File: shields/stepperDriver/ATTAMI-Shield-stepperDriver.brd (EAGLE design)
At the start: 22.8 x 33 mm, 12 parts

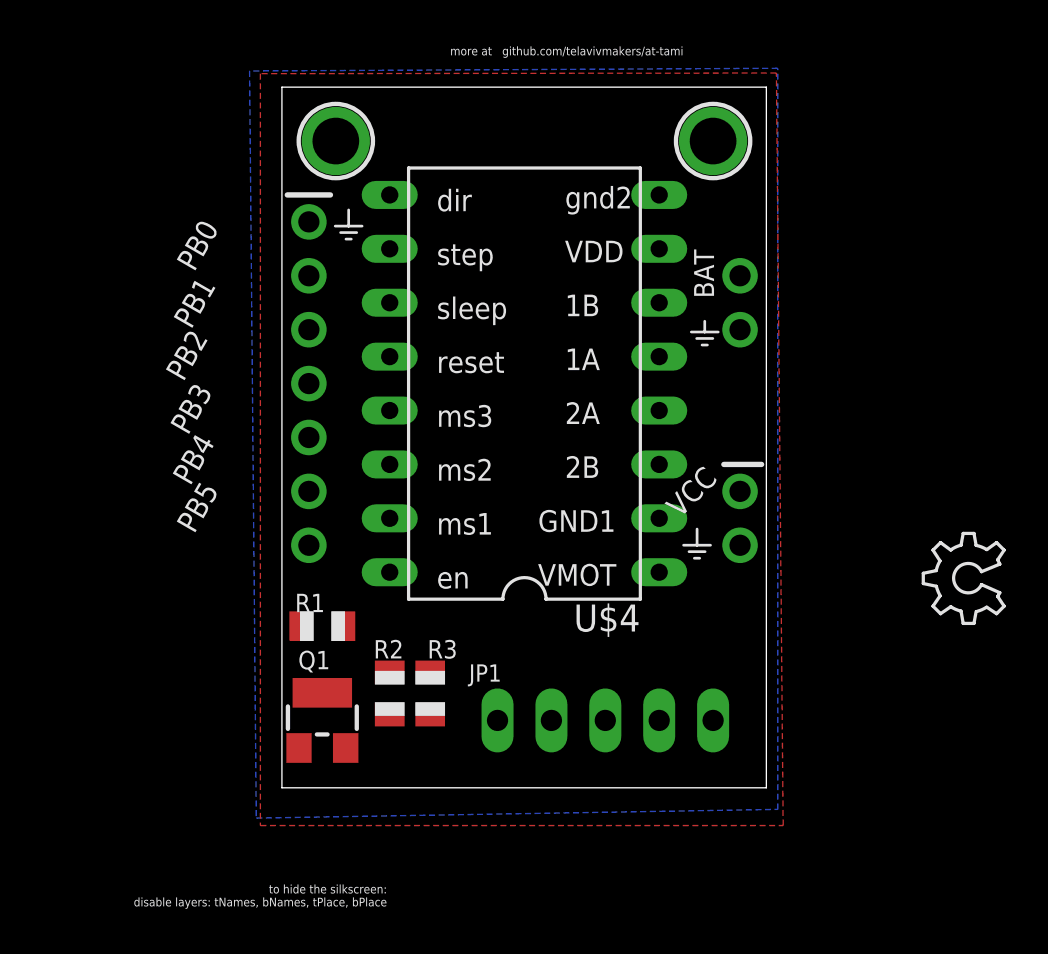
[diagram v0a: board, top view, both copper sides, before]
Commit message: cont work on stepper shield
mostly done, could work if we agree on V_BAT to 12V
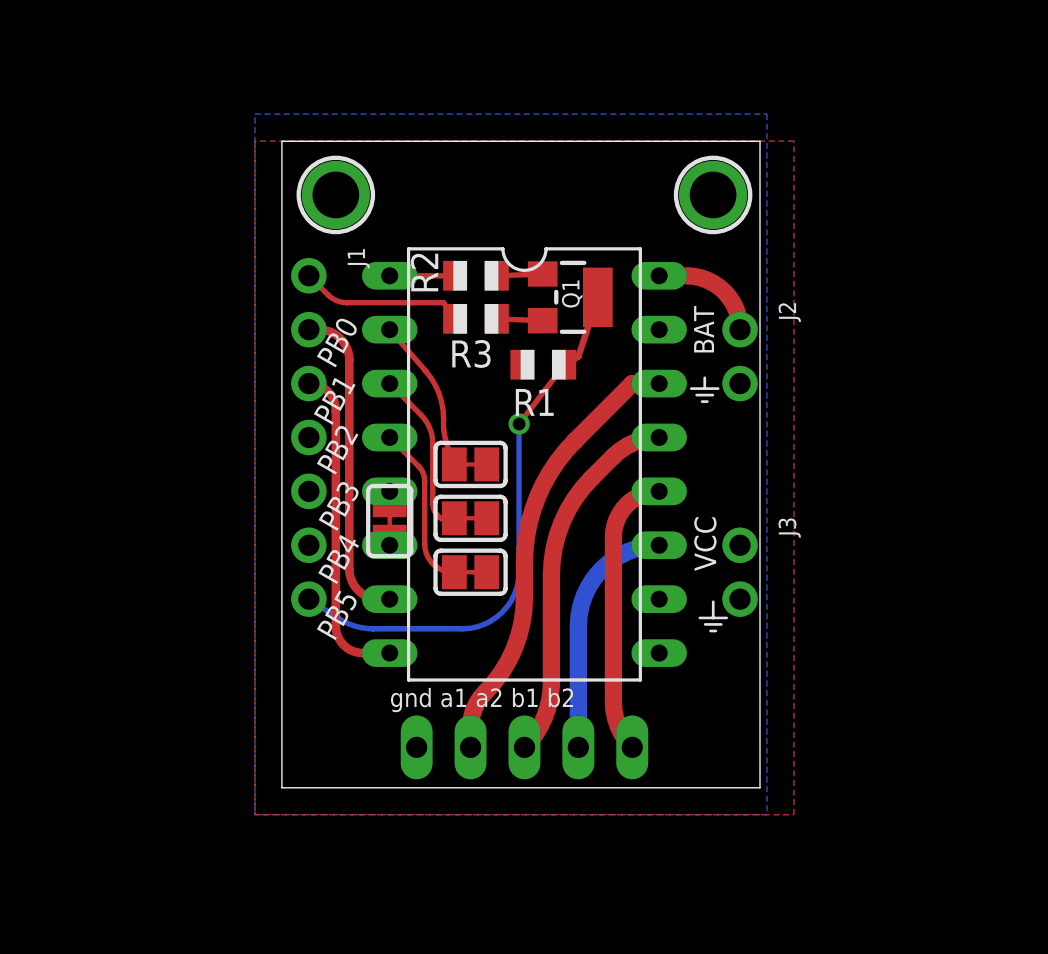
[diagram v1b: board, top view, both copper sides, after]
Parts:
- removed U$4: POLOLUESTEPPERDRIVER, reprap:DIL16
- added SJ1, SJ2, SJ3, SJ4: (no value), microbuilder:SOLDERJUMPER_CLOSEDWIRE
- U$3: value (none) -> STEPPER_driver; device ohw-logo:OSHW_6X150_NOTEXT -> ATtami:DIL16
- moved U$3 23.8 mm to (11.4, 15.2), turned to 0 degrees
- moved Q1 23.1 mm to (13.6, 23.1), turned to 270 degrees
- moved R2 20.1 mm to (9.14, 24.1), turned to 0 degrees
- moved U$1 18.0 mm to (20.3, 27.9), turned to 0 degrees
- moved U$2 18.0 mm to (2.54, 27.9)
- moved R3 17.8 mm to (9.14, 22.1), turned to 0 degrees
- moved R1 16.1 mm to (12.3, 19.9), turned to 0 degrees
- moved JP1 4.02 mm to (11.4, 1.91)
- moved J1 2.54 mm to (1.27, 16.5)
- moved J2 2.54 mm to (21.6, 20.3)
- moved J3 2.54 mm to (21.6, 10.2)
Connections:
- removed net EN: R2.1, U$4.16
- removed net N$11: JP1.2, U$4.5
- new net ENABLE: R2.1, U$3.1
- new net N$14: SJ1.2, U$3.4
- new net N$2: SJ4.2, U$3.5
- new net N$3: JP1.2, U$3.11
- new net N$6: JP1.3, U$3.12
- new net N$7: JP1.4, U$3.14
- new net N$9: SJ4.1, U$3.6
- net GND: now also JP1.1, U$3.10, U$3.16; no longer U$4.2, U$4.8
- net N$10: now also SJ3.2, U$3.2; no longer JP1.3, U$4.4
- net N$13: now also SJ2.2, U$3.3; no longer JP1.1, U$4.6
- net N$8: now also JP1.5, U$3.13; no longer JP1.4, U$4.3
- net PB0: now also U$3.7; no longer U$4.9
- net PB1: now also U$3.8; no longer U$4.10
- net VCC: now also SJ1.1, SJ2.1, SJ3.1, U$3.15; no longer U$4.7
- net V_BAT: now also U$3.9; no longer JP1.5, U$4.1
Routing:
- net PB5: track 0.00 -> 25.5 mm, vias 0 -> 1
- net N$3: track 0.00 -> 21.1 mm
- net N$6: track 0.00 -> 17.1 mm
- net PB1: track 0.00 -> 15.0 mm
- net PB0: track 0.00 -> 14.8 mm
- net N$8: track 0.00 -> 13.1 mm
- net N$7: track 0.00 -> 11.1 mm
- net N$13: track 0.00 -> 7.77 mm
- net GND: track 0.00 -> 7.72 mm
- net N$14: track 0.00 -> 7.59 mm
- net N$10: track 0.00 -> 7.21 mm
- net V_BAT: track 0.00 -> 3.59 mm
- net ENABLE: track 0.00 -> 3.06 mm
- net N$5: track 0.00 -> 2.15 mm
- net N$4: track 0.00 -> 2.15 mm
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- added copper zone on layer 1, net VCC
- removed copper zone on layer 1, net GND
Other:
- board size 22.8 x 33 mm -> 22.5 x 30.5 mm
- board text added: "gnd a1 a2 b1 b2"
- board text removed: "+"
- board text removed: "1A"
- board text removed: "1B"
- board text removed: "2A"
- board text removed: "2B"
- board text removed: "GND1"
- board text removed: "J2"
- board text removed: "VDD"
- board text removed: "VMOT"
- board text removed: "dir"
- board text removed: "en"
- board text removed: "gnd2"
- board text removed: "more at github.com/telavivmakers/at-tami"
- board text removed: "ms1"
- board text removed: "ms2"
- board text removed: "ms3"
- board text removed: "reset"
- board text removed: "sleep"
- board text removed: "step"
- board text removed: "to hide the silkscreen: disable layers: tNames, bNames, tPlace, bPlace"

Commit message: updtae A4988 lib part
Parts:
- BRK1: value STEPPER_driver -> A4988_driver
- moved R1 2.68 mm to (9.65, 19.7)
- moved R3 0.52 mm to (9.65, 22.0)
- moved R2 0.40 mm to (9.53, 24.3)
- renumbered U$3 to BRK1
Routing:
- net PB5: track 25.5 -> 27.0 mm
- net N$4: track 2.15 -> 1.64 mm
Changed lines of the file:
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@@
 <attribute name="VALUE" x="12.954" y="21.082" size="0.4064" layer="27" ratio="10" rot="R270"/>
 </element>
-<element name="R1" library="adafruit" package="R0805" value="" x="12.319" y="19.939" smashed="yes">
-<attribute name="NAME" x="12.954" y="18.796" size="1.27" layer="25" rot="R180"/>
-<attribute name="VALUE" x="11.557" y="17.653" size="1.27" layer="27"/>
-</element>
-<element name="R2" library="adafruit" package="R0805" value="" x="9.144" y="24.13" smashed="yes">
-<attribute name="NAME" x="7.366" y="23.241" size="1.27" layer="25" rot="R90"/>
-<attribute name="VALUE" x="8.382" y="21.844" size="1.27" layer="27"/>
-</element>
-<element name="R3" library="adafruit" package="R0805" value="" x="9.144" y="22.098" smashed="yes">
-<attribute name="NAME" x="7.874" y="19.812" size="1.27" layer="25"/>
-<attribute name="VALUE" x="8.382" y="19.812" size="1.27" layer="27"/>
+<element name="R1" library="adafruit" package="R0805" value="" x="9.652" y="19.685" smashed="yes">
+<attribute name="NAME" x="11.811" y="20.701" size="1.016" layer="25" rot="R270"/>
+<attribute name="VALUE" x="8.89" y="17.399" size="1.27" layer="27"/>
+</element>
+<element name="R2" library="adafruit" package="R0805" value="" x="9.525" y="24.257" smashed="yes">
+<attribute name="NAME" x="7.874" y="23.495" size="1.016" layer="25" rot="R90"/>
+<attribute name="VALUE" x="8.763" y="21.971" size="1.27" layer="27"/>
+</element>
+<element name="R3" library="adafruit" package="R0805" value="" x="9.652" y="21.971" smashed="yes">
+<attribute name="NAME" x="7.874" y="21.336" size="1.016" layer="25" rot="R90"/>
+<attribute name="VALUE" x="8.89" y="19.685" size="1.27" layer="27"/>
 </element>
 <element name="SJ1" library="microbuilder" package="SOLDERJUMPER_CLOSEDWIRE" value="" x="8.89" y="10.16" smashed="yes" rot="R180">
@@
 <element name="U$1" library="microbuilder" package="MOUNTINGHOLE_2.0_PLATED" value="MOUNTINGHOLE2.0" x="20.32" y="27.94"/>
 <element name="U$2" library="microbuilder" package="MOUNTINGHOLE_2.0_PLATED" value="MOUNTINGHOLE2.0" x="2.54" y="27.94"/>
-<element name="U$3" library="ATtami" package="DIL16" value="STEPPER_driver" x="11.43" y="15.24" smashed="yes">
+<element name="BRK1" library="ATtami" package="DIL16" value="A4988_driver" x="11.43" y="15.24" smashed="yes">
 <attribute name="VALUE" x="15.875" y="5.334" size="1.27" layer="27" ratio="10" rot="R90"/>
 </element>
@@
 <contactref element="J1" pad="1"/>
 <contactref element="R3" pad="1"/>
-<contactref element="U$3" pad="16"/>
+<contactref element="BRK1" pad="16"/>
 <polygon width="0.4064" layer="16">
 <vertex x="-1.27" y="31.75"/>
@@
 <vertex x="-1.27" y="-1.27"/>
 </polygon>
-<wire x1="7.62" y1="22.86" x2="3.06605" y2="22.86" width="0.254" layer="1"/>
+<wire x1="3.06605" y1="22.86" x2="6.975896875" y2="22.86" width="0.254" layer="1"/>
+<wire x1="6.975896875" y1="22.86" x2="8.00054375" y2="22.34033125" width="0.254" layer="1" curve="-53.785325"/>
+<wire x1="8.00054375" y1="22.34033125" x2="8.652" y2="21.971" width="0.254" layer="1"/>
 <wire x1="3.06605" y1="22.86" x2="2.168025" y2="23.231975" width="0.254" layer="1" curve="-45"/>
 <wire x1="2.168025" y1="23.231975" x2="1.27" y2="24.13" width="0.254" layer="1"/>
-<contactref element="U$3" pad="10"/>
+<contactref element="BRK1" pad="10"/>
 <contactref element="JP1" pad="1"/>
-<wire x1="7.62" y1="22.86" x2="8.144" y2="22.098" width="0.254" layer="1"/>
 </signal>
 <signal name="VCC">
 <contactref element="J3" pad="1"/>
 <contactref element="R1" pad="1"/>
-<contactref element="U$3" pad="15"/>
+<contactref element="BRK1" pad="15"/>
 <contactref element="SJ1" pad="1"/>
 <contactref element="SJ2" pad="1"/>
@@
 <contactref element="J2" pad="1"/>
 <wire x1="19.05" y1="24.13" x2="21.59" y2="21.59" width="0.8128" layer="1" curve="-90"/>
-<contactref element="U$3" pad="9"/>
+<contactref element="BRK1" pad="9"/>
 <wire x1="17.78" y1="24.13" x2="19.05" y2="24.13" width="0" layer="19" extent="1-1"/>
 </signal>
 <signal name="PB0">
 <contactref element="J1" pad="2"/>
-<contactref element="U$3" pad="7"/>
+<contactref element="BRK1" pad="7"/>
 <wire x1="1.27" y1="21.59" x2="1.755096875" y2="21.59" width="0.4064" layer="1"/>
 <wire x1="1.755096875" y1="21.59" x2="3.175" y2="20.170096875" width="0.4064" layer="1" curve="-90"/>
@@
 <signal name="PB1">
 <contactref element="J1" pad="3"/>
-<contactref element="U$3" pad="8"/>
+<contactref element="BRK1" pad="8"/>
 <wire x1="1.27" y1="19.05" x2="2.54" y2="17.78" width="0.4064" layer="1" curve="-90"/>
 <wire x1="2.54" y1="17.78" x2="2.54" y2="7.62" width="0.4064" layer="1"/>
@@
 <contactref element="Q1" pad="3"/>
 <contactref element="J1" pad="7"/>
-<wire x1="13.319" y1="19.939" x2="11.176" y2="17.145" width="0.254" layer="1"/>
+<wire x1="10.652" y1="19.685" x2="11.176" y2="17.145" width="0.254" layer="1"/>
 <via x="11.176" y="17.145" extent="1-16" drill="0.6" shape="square"/>
 <wire x1="11.176" y1="17.145" x2="11.176" y2="10.172065625" width="0.254" layer="16"/>
@@
 <wire x1="4.292428125" y1="7.493" x2="2.704090625" y2="7.962059375" width="0.254" layer="16" curve="-32.905279"/>
 <wire x1="2.704090625" y1="7.962059375" x2="1.27" y2="8.89" width="0.254" layer="16"/>
-<wire x1="14.889" y1="23.114" x2="13.97" y2="20.32" width="0.3048" layer="1"/>
-<wire x1="13.97" y1="20.32" x2="13.319" y2="19.939" width="0.3048" layer="1"/>
+<wire x1="14.889" y1="23.114" x2="14.3002875" y2="21.324159375" width="0.3048" layer="1"/>
+<wire x1="14.3002875" y1="21.324159375" x2="12.931759375" y2="20.1213" width="0.3048" layer="1" curve="-60.958763"/>
+<wire x1="12.931759375" y1="20.1213" x2="10.652" y2="19.685" width="0.3048" layer="1"/>
 </signal>
 <signal name="N$4">
 <contactref element="R3" pad="2"/>
 <contactref element="Q1" pad="2"/>
-<wire x1="12.289" y1="22.014" x2="10.144" y2="22.098" width="0.254" layer="1"/>
+<wire x1="12.289" y1="22.014" x2="10.652" y2="21.971" width="0.254" layer="1"/>
 </signal>
 <signal name="N$5">
 <contactref element="Q1" pad="1"/>
 <contactref element="R2" pad="2"/>
-<wire x1="10.144" y1="24.13" x2="12.289" y2="24.214" width="0.254" layer="1"/>
+<wire x1="10.525" y1="24.257" x2="12.289" y2="24.214" width="0.254" layer="1"/>
 </signal>
 <signal name="ENABLE">
 <contactref element="R2" pad="1"/>
-<contactref element="U$3" pad="1"/>
-<wire x1="5.08" y1="24.13" x2="8.144" y2="24.13" width="0.254" layer="1"/>
+<contactref element="BRK1" pad="1"/>
+<wire x1="5.08" y1="24.13" x2="8.525" y2="24.257" width="0.254" layer="1"/>
 </signal>
 <signal name="N$10">
 <contactref element="SJ3" pad="2"/>
-<contactref element="U$3" pad="2"/>
+<contactref element="BRK1" pad="2"/>
 <wire x1="8.128" y1="15.24" x2="8.063171875" y2="15.434484375" width="0.254" layer="1"/>
 <wire x1="8.063171875" y1="15.434484375" x2="7.62" y2="16.89543125" width="0.254" layer="1" curve="-18.434976"/>
@@
 <signal name="N$13">
 <contactref element="SJ2" pad="2"/>
-<contactref element="U$3" pad="3"/>
+<contactref element="BRK1" pad="3"/>
 <wire x1="8.128" y1="12.7" x2="7.92519375" y2="12.573" width="0.254" layer="1"/>
 <wire x1="7.92519375" y1="12.573" x2="7.112" y2="13.38619375" width="0.254" layer="1" curve="-90"/>
@@
 <signal name="N$14">
 <contactref element="SJ1" pad="2"/>
-<contactref element="U$3" pad="4"/>
+<contactref element="BRK1" pad="4"/>
 <wire x1="5.08" y1="16.51" x2="6.4477125" y2="15.1422875" width="0.254" layer="1"/>
 <wire x1="6.4477125" y1="15.1422875" x2="6.731" y2="14.458371875" width="0.254" layer="1" curve="-45"/>
@@
 <signal name="N$3">
 <contactref element="JP1" pad="2"/>
-<contactref element="U$3" pad="11"/>
+<contactref element="BRK1" pad="11"/>
 <wire x1="17.78" y1="19.05" x2="16.51" y2="19.05" width="0.8128" layer="1"/>
 <wire x1="16.51" y1="19.05" x2="13.811796875" y2="16.351796875" width="0.8128" layer="1"/>
@@
 <signal name="N$6">
 <contactref element="JP1" pad="3"/>
-<contactref element="U$3" pad="12"/>
+<contactref element="BRK1" pad="12"/>
 <wire x1="17.78" y1="16.51" x2="15.611975" y2="15.611975" width="0.8128" layer="1" curve="45"/>
 <wire x1="15.611975" y1="15.611975" x2="14.596703125" y2="14.596703125" width="0.8128" layer="1"/>
@@
 <signal name="N$7">
 <contactref element="JP1" pad="4"/>
-<contactref element="U$3" pad="14"/>
+<contactref element="BRK1" pad="14"/>
 <wire x1="17.78" y1="11.43" x2="13.97" y2="7.62" width="0.8128" layer="16" curve="90"/>
 <wire x1="13.97" y1="7.62" x2="13.97" y2="1.905" width="0.8128" layer="16"/>
@@
 <signal name="N$8">
 <contactref element="JP1" pad="5"/>
-<contactref element="U$3" pad="13"/>
+<contactref element="BRK1" pad="13"/>
 <wire x1="17.78" y1="13.97" x2="15.621" y2="11.811" width="0.8128" layer="1" curve="90"/>
 <wire x1="15.621" y1="11.811" x2="15.621" y2="4.051234375" width="0.8128" layer="1"/>
@@
 </signal>
 <signal name="N$2">
-<contactref element="U$3" pad="5"/>
+<contactref element="BRK1" pad="5"/>
 <contactref element="SJ4" pad="2"/>
 <wire x1="5.08" y1="13.335" x2="5.08" y2="13.97" width="0.4064" layer="1"/>
@@
 <signal name="N$9">
 <contactref element="SJ4" pad="1"/>
-<contactref element="U$3" pad="6"/>
+<contactref element="BRK1" pad="6"/>
 <wire x1="5.08" y1="11.43" x2="5.08" y2="11.811" width="0.4064" layer="1"/>
 </signal>

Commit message: addded 4pin header for 12+ and I2C, not routed
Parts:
- added CN1: 1X4-BIG, adafruit:1X04-BIG
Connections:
- net GND: now also CN1.2
- net PB3: now also CN1.4
- net PB4: now also CN1.3
- net V_BAT: now also CN1.1
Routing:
- net V_BAT: track 3.59 -> 8.17 mm
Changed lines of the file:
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@@
 <attribute name="VALUE" x="6.731" y="11.049" size="0.4064" layer="27" ratio="10" rot="R90"/>
 </element>
+<element name="CN1" library="adafruit" package="1X04-BIG" value="1X4-BIG" x="15.24" y="27.94" smashed="yes" rot="R180"/>
 </elements>
 <signals>
@@
 <contactref element="BRK1" pad="10"/>
 <contactref element="JP1" pad="1"/>
+<contactref element="CN1" pad="2"/>
 </signal>
 <signal name="VCC">
@@
 <wire x1="19.05" y1="24.13" x2="21.59" y2="21.59" width="0.8128" layer="1" curve="-90"/>
 <contactref element="BRK1" pad="9"/>
+<contactref element="CN1" pad="1"/>
+<wire x1="15.24" y1="27.94" x2="17.78" y2="24.13" width="0.8128" layer="1"/>
 <wire x1="17.78" y1="24.13" x2="19.05" y2="24.13" width="0" layer="19" extent="1-1"/>
 </signal>
@@
 <signal name="PB3">
 <contactref element="J1" pad="5"/>
+<contactref element="CN1" pad="4"/>
+<wire x1="1.27" y1="13.97" x2="7.62" y2="27.94" width="0" layer="19" extent="1-1"/>
 </signal>
 <signal name="PB4">
 <contactref element="J1" pad="6"/>
+<contactref element="CN1" pad="3"/>
+<wire x1="1.27" y1="11.43" x2="10.16" y2="27.94" width="0" layer="19" extent="1-1"/>
 </signal>
 <signal name="PB5">

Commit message: updated wiring, needs review
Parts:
- moved R1 0.25 mm to (9.65, 19.4), turned to 180 degrees
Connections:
- net N$7: now also BRK1.13; no longer BRK1.14
- net N$8: now also BRK1.14; no longer BRK1.13
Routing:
- net VCC: track 0.00 -> 28.6 mm, vias 0 -> 2
- net PB4: track 0.00 -> 22.6 mm
- net PB3: track 0.00 -> 18.1 mm
- net N$7: track 11.1 -> 14.8 mm
- net N$8: track 13.1 -> 11.7 mm
- net V_BAT: track 8.17 -> 9.44 mm
- net N$3: track 21.1 -> 22.3 mm
- net N$6: track 17.1 -> 18.1 mm
- net PB5: track 27.0 -> 26.1 mm
- added copper zone on layer 1, net GND
- removed copper zone on layer 1, net VCC
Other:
- board text added: "GND 2B 2A 1A 1B"
- board text added: "i2c i2c GND VMOT"
- board text removed: "gnd a1 a2 b1 b2"
